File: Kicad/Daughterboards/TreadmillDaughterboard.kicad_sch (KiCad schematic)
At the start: 26 parts, among them J13 RJ45, J14 Conn_01x03_Socket, J15 Conn_01x03_Socket, SW7 SW_Push_Open_Dual, SW8 SW_Push_Open_Dual, U3 DRV5033AJxLPG

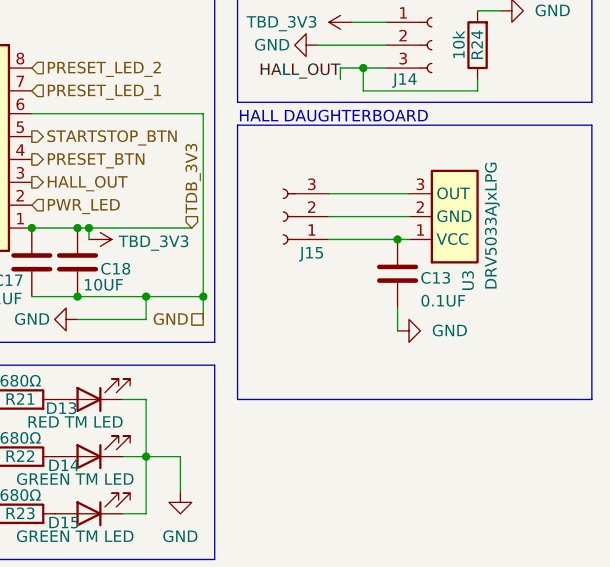
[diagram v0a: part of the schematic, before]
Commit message: Finished project
Made daughterboard pcbs, fixed silkscreen errors on mainboard pcb, generated GERBERs and drill files
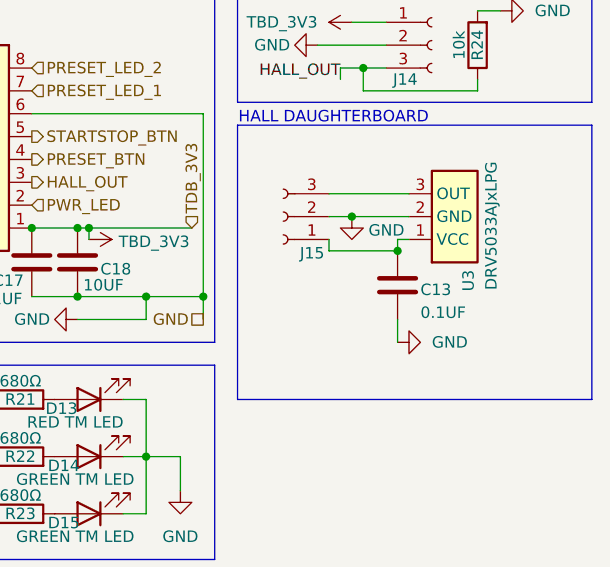
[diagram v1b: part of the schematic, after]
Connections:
- net GND: now also J15.2 (Pin_2), U3.2 (GND)
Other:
- moved on the sheet: C13
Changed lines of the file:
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@@
+	)
+	(junction
+		(at 71.12 40.64)
+		(diameter 0)
+		(color 0 0 0 0)
 	)
 	(junction
@@
 	)
 	(junction
-		(at 76.2 43.18)
-		(diameter 0)
-		(color 0 0 0 0)
-	)
-	(junction
 		(at 39.37 90.17)
 		(diameter 0)
@@
 	)
 	(junction
+		(at 76.2 44.45)
+		(diameter 0)
+		(color 0 0 0 0)
+	)
+	(junction
 		(at 41.91 41.91)
 		(diameter 0)
@@
 	(wire
 		(pts
-			(xy 68.58 40.64) (xy 77.47 40.64)
+			(xy 68.58 40.64) (xy 71.12 40.64)
 		)
 		(stroke
@@
 	(wire
 		(pts
-			(xy 68.58 43.18) (xy 76.2 43.18)
+			(xy 68.58 44.45) (xy 76.2 44.45)
 		)
 		(stroke
@@
 	(wire
 		(pts
+			(xy 76.2 44.45) (xy 76.2 43.18)
+		)
+		(stroke
+			(width 0)
+			(type default)
+		)
+	)
+	(wire
+		(pts
 			(xy 39.37 100.33) (xy 39.37 101.6)
 		)
@@
 	(wire
 		(pts
-			(xy 76.2 50.8) (xy 76.2 53.34)
+			(xy 76.2 52.07) (xy 76.2 54.61)
 		)
 		(stroke
@@
 	(wire
 		(pts
+			(xy 71.12 40.64) (xy 77.47 40.64)
+		)
+		(stroke
+			(width 0)
+			(type default)
+		)
+	)
+	(wire
+		(pts
 			(xy 39.37 90.17) (xy 41.91 90.17)
 		)
@@
 		(pts
 			(xy 52.07 85.09) (xy 52.07 90.17)
+		)
+		(stroke
+			(width 0)
+			(type default)
+		)
+	)
+	(wire
+		(pts
+			(xy 68.58 44.45) (xy 68.58 43.18)
 		)
 		(stroke
@@
 	(symbol
 		(lib_id "power:GND")
-		(at 76.2 53.34 90)
+		(at 76.2 54.61 90)
 		(unit 1)
 		(body_style 1)
@@
 		(fields_autoplaced yes)
 		(property "Reference" "#PWR057"
-			(at 82.55 53.34 0)
+			(at 82.55 54.61 0)
 			(hide yes)
 			(show_name no)
@@
 		)
 		(property "Value" "GND"
-			(at 80.01 53.3399 90)
+			(at 80.01 54.6099 90)
 			(show_name no)
 			(do_not_autoplace no)
@@
 		)
 		(property "Footprint" ""
-			(at 76.2 53.34 0)
+			(at 76.2 54.61 0)
 			(hide yes)
 			(show_name no)
@@
 		)
 		(property "Datasheet" ""
-			(at 76.2 53.34 0)
+			(at 76.2 54.61 0)
 			(hide yes)
 			(show_name no)
@@
 		)
 		(property "Description" "Power symbol creates a global label with name \"GND\" , ground"
-			(at 76.2 53.34 0)
+			(at 76.2 54.61 0)
 			(hide yes)
 			(show_name no)
@@
 	)
 	(symbol
+		(lib_id "power:GND")
+		(at 71.12 40.64 0)
+		(unit 1)
+		(body_style 1)
+		(exclude_from_sim no)
+		(in_bom yes)
+		(on_board yes)
+		(in_pos_files yes)
+		(dnp no)
+		(property "Reference" "#PWR058"
+			(at 71.12 46.99 0)
+			(hide yes)
+			(show_name no)
+			(do_not_autoplace no)
+			(effects
+				(font
+					(size 1.27 1.27)
+				)
+			)
+		)
+		(property "Value" "GND"
+			(at 76.962 42.164 0)
+			(show_name no)
+			(do_not_autoplace no)
+			(effects
+				(font
+					(size 1.27 1.27)
+				)
+				(justify right)
+			)
+		)
+		(property "Footprint" ""
+			(at 71.12 40.64 0)
+			(hide yes)
+			(show_name no)
+			(do_not_autoplace no)
+			(effects
+				(font
+					(size 1.27 1.27)
+				)
+			)
+		)
+		(property "Datasheet" ""
+			(at 71.12 40.64 0)
+			(hide yes)
+			(show_name no)
+			(do_not_autoplace no)
+			(effects
+				(font
+					(size 1.27 1.27)
+				)
+			)
+		)
+		(property "Description" "Power symbol creates a global label with name \"GND\" , ground"
+			(at 71.12 40.64 0)
+			(hide yes)
+			(show_name no)
+			(do_not_autoplace no)
+			(effects
+				(font
+					(size 1.27 1.27)
+				)
+			)
+		)
+		(pin "1"
+		)
+		(instances
+			(project "FluxCapacitor"
+				(path "/feb6d8df-599a-4f82-8f89-f7a3c96de191/2034eb13-da9e-4ee9-8d15-531e4404cdd1"
+					(reference "#PWR058")
+					(unit 1)
+				)
+			)
+		)
+	)
+	(symbol
 		(lib_id "power:+3V3")
 		(at 71.12 19.05 90)
@@
 	(symbol
 		(lib_id "Device:C")
-		(at 76.2 46.99 0)
+		(at 76.2 48.26 0)
 		(unit 1)
 		(body_style 1)
@@
 		(dnp no)
 		(property "Reference" "C13"
-			(at 78.74 47.498 0)
+			(at 78.74 48.768 0)
 			(show_name no)
 			(do_not_autoplace no)
@@
 		)
 		(property "Value" "0.1UF"
-			(at 78.74 50.038 0)
+			(at 78.74 51.308 0)
 			(show_name no)
 			(do_not_autoplace no)
@@
 		)
 		(property "Footprint" "FluxCapacitor:CC0805KRX7R9BB104"
-			(at 77.1652 50.8 0)
+			(at 77.1652 52.07 0)
 			(hide yes)
 			(show_name no)
@@
 		)
 		(property "Datasheet" ""
-			(at 76.2 46.99 0)
+			(at 76.2 48.26 0)
 			(hide yes)
 			(show_name no)
@@
 		)
 		(property "Description" "Unpolarized capacitor"
-			(at 76.2 46.99 0)
-			(hide yes)
-			(show_name no)
+			(at 76.2 48.26 0)
+			(hide yes)
+			(show_name no)
